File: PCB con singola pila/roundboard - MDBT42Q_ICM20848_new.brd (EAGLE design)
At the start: 36.6 x 20.8 mm, 24 parts, among them U1 ICM-20948, U3 ADP1606ACPZN1.8-R7CP_6_3_ADI-L, X2 32.768kHz

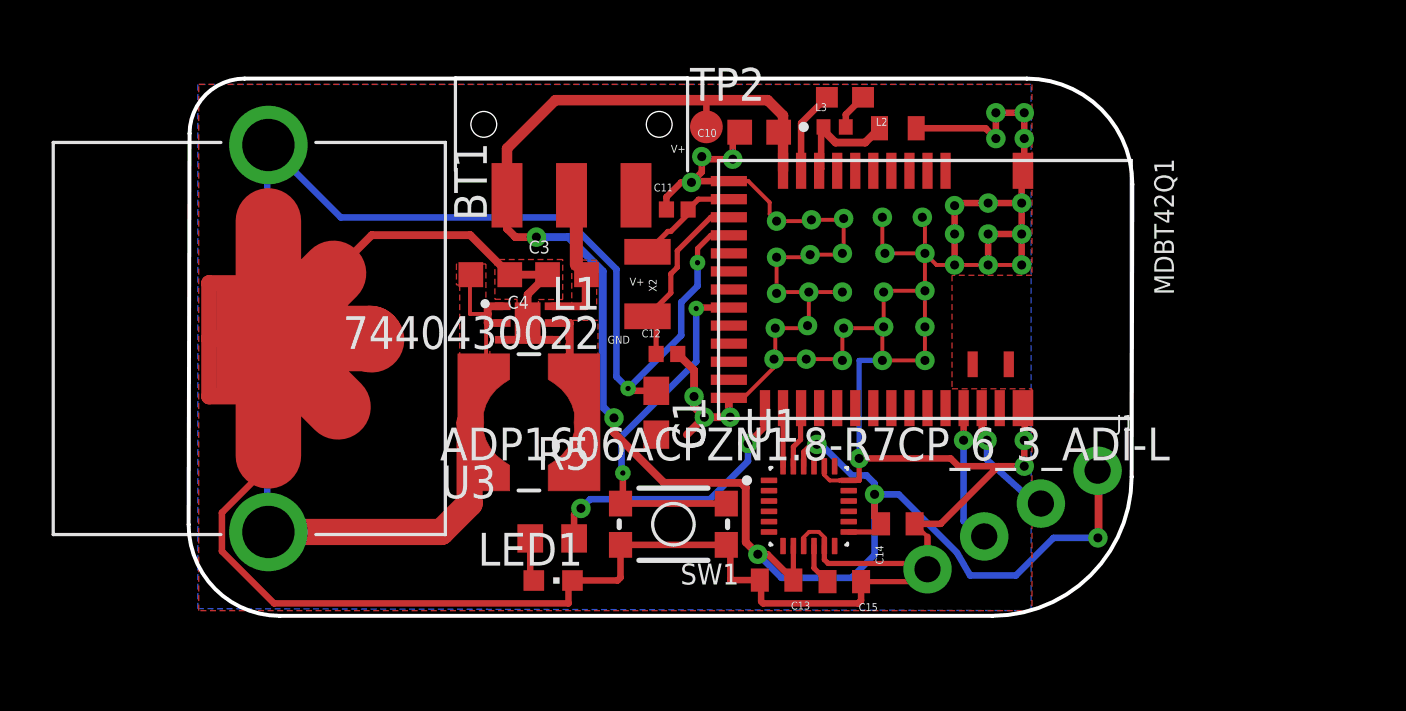
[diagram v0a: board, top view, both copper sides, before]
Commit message: Led più grande (1206)
Tolti anche vari componenti inutili come le resistenze di pull up per i2c (già integrate nell'nrf) e la resistenza su INT dell'ICM
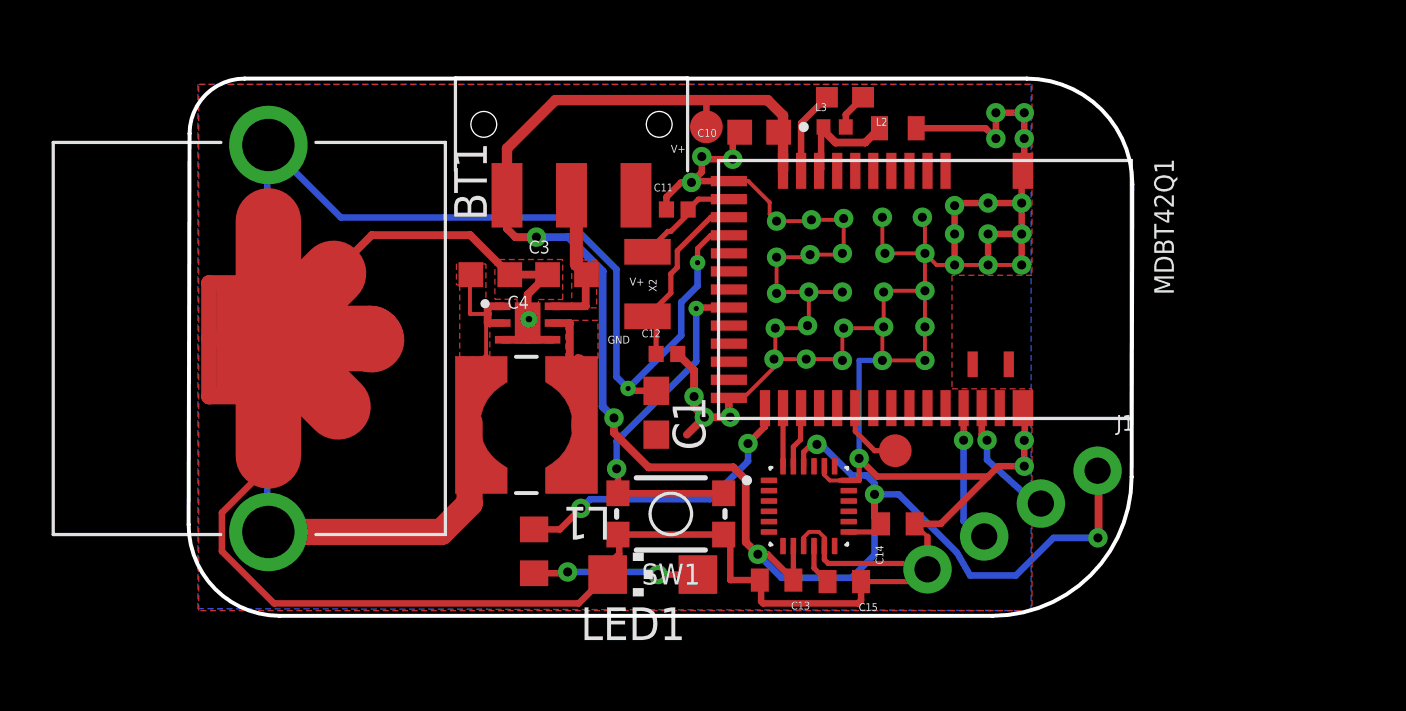
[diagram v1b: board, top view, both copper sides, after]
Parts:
- added UART_TP: TPB1,27, testpad:B1,27
- LED1: device led:CHIPLED_0603 -> led:CHIPLED_1206
- moved LED1 3.87 mm to (10.1, 3.10), turned to 90 degrees
- moved R5 0.86 mm to (5.50, 4.00), turned to 90 degrees
- moved SW1 0.41 mm to (10.8, 5.45)
- moved L1 0.14 mm to (5.20, 8.90)
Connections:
- net P0.16: now also UART_TP.TP
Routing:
- net N$1: track 1.69 -> 6.41 mm, vias 0 -> 2
- net P0.16: track 0.00 -> 2.76 mm
- net IND: track 5.20 -> 3.02 mm
- net V+BATT: track 65.6 -> 63.7 mm
- net N$5: track 10.9 -> 11.7 mm
- net GND: track 185.6 -> 185.4 mm, vias 47 -> 48

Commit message: Aggiunte versioni con 2 pile
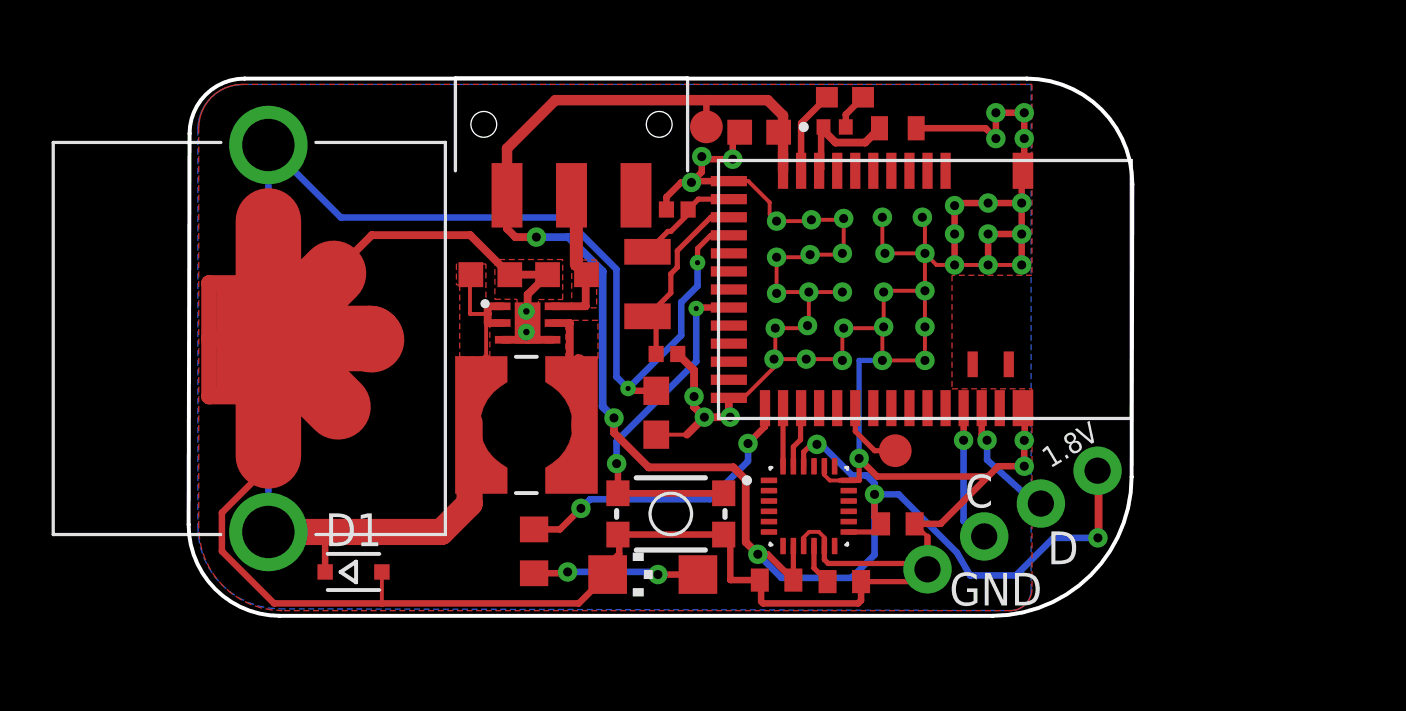
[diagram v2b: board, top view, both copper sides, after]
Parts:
- added D1: (no value), diode:SOD323-R
- renumbered TP2 to 1.8V_TP
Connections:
- net GND: now also D1.A
- net V+BATT: now also D1.C
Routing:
- net GND: track 185.4 -> 188.6 mm, vias 48 -> 49
- net V+BATT: track 63.7 -> 66.5 mm
- net IND: track 3.02 -> 5.30 mm
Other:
- board text added: "1.8V"
- board text added: "C"
- board text added: "D"
- board text removed: "V+"
